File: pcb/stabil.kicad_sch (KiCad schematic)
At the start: 44 parts, among them Q10 IRFR5305, U11 TPS5430DDA, U12 LM75B, U13 INA219AxD, U14 LM78M05_TO252, U16 TSV911IDT, U17 PC817

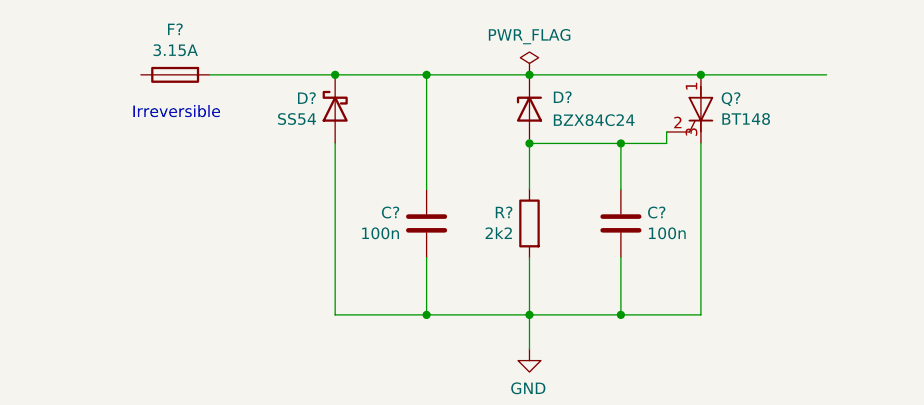
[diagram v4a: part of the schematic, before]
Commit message: Use normal SMD footprints, avoid handsolder.
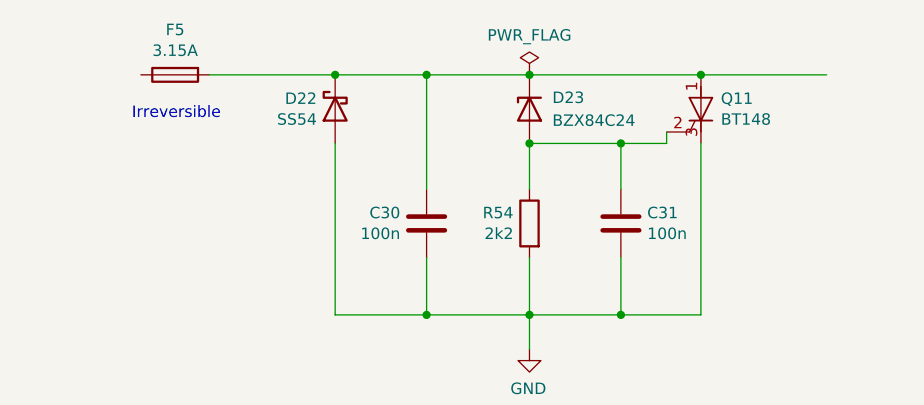
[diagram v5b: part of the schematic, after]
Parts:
- C14, C19, C21, C23, C24, C26, C27, C28: footprint Capacitor_SMD:C_0805_2012Metric_Pad1.18x1.45mm_HandSolder -> Capacitor_SMD:C_0805_2012Metric
- C30, C31: renamed from C?; footprint Capacitor_SMD:C_0805_2012Metric_Pad1.18x1.45mm_HandSolder -> Capacitor_SMD:C_0805_2012Metric
- D17: footprint Diode_SMD:D_SMA_Handsoldering -> Diode_SMD:D_SMA
- D22: renamed from D?; footprint Diode_SMD:D_SMA_Handsoldering -> Diode_SMD:D_SMA
- R30, R33, R44, R45, R46, R52, R53, R56, R57, R58: footprint Resistor_SMD:R_0805_2012Metric_Pad1.20x1.40mm_HandSolder -> Resistor_SMD:R_0805_2012Metric
- R43, R55: footprint Resistor_SMD:R_2512_6332Metric_Pad1.40x3.35mm_HandSolder -> Resistor_SMD:R_2512_6332Metric
- R54: renamed from R?; footprint Resistor_SMD:R_0805_2012Metric_Pad1.20x1.40mm_HandSolder -> Resistor_SMD:R_0805_2012Metric
- gave numbers to parts that had none: 3
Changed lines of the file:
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@@
 			)
 		)
-		(property "Footprint" "Resistor_SMD:R_0805_2012Metric_Pad1.20x1.40mm_HandSolder"
+		(property "Footprint" "Resistor_SMD:R_0805_2012Metric"
 			(at 202.692 36.83 90)
 			(effects
@@
 			)
 		)
-		(property "Footprint" "Resistor_SMD:R_0805_2012Metric_Pad1.20x1.40mm_HandSolder"
+		(property "Footprint" "Resistor_SMD:R_0805_2012Metric"
 			(at 223.012 36.83 90)
 			(effects
@@
 		(on_board yes)
 		(dnp no)
-		(property "Reference" "Q?"
+		(property "Reference" "Q11"
 			(at 215.5698 -37.9984 0)
 			(effects
@@
 			(project ""
 				(path "/99e6b8eb-b08e-4d42-84dd-8b7f6765b7b7/00000000-0000-0000-0000-000062367840"
-					(reference "Q?")
+					(reference "Q11")
 					(unit 1)
 				)
@@
 		(on_board yes)
 		(dnp no)
-		(property "Reference" "C?"
+		(property "Reference" "C31"
 			(at 207.391 -25.2984 0)
 			(effects
@@
 			)
 		)
-		(property "Footprint" "Capacitor_SMD:C_0805_2012Metric_Pad1.18x1.45mm_HandSolder"
+		(property "Footprint" "Capacitor_SMD:C_0805_2012Metric"
 			(at 203.5048 -27.94 0)
 			(effects
@@
 			(project ""
 				(path "/99e6b8eb-b08e-4d42-84dd-8b7f6765b7b7/00000000-0000-0000-0000-000062367840"
-					(reference "C?")
+					(reference "C31")
 					(unit 1)
 				)
@@
 		(on_board yes)
 		(dnp no)
-		(property "Reference" "R?"
+		(property "Reference" "R54"
 			(at 192.532 -25.2984 0)
 			(effects
@@
 			)
 		)
-		(property "Footprint" "Resistor_SMD:R_0805_2012Metric_Pad1.20x1.40mm_HandSolder"
+		(property "Footprint" "Resistor_SMD:R_0805_2012Metric"
 			(at 196.088 -24.13 90)
 			(effects
@@
 			(project ""
 				(path "/99e6b8eb-b08e-4d42-84dd-8b7f6765b7b7/00000000-0000-0000-0000-000062367840"
-					(reference "R?")
+					(reference "R54")
 					(unit 1)
 				)
@@
 		(on_board yes)
 		(dnp no)
-		(property "Reference" "C?"
+		(property "Reference" "C30"
 			(at 179.959 -25.2984 0)
 			(effects
@@
 			)
 		)
-		(property "Footprint" "Capacitor_SMD:C_0805_2012Metric_Pad1.18x1.45mm_HandSolder"
+		(property "Footprint" "Capacitor_SMD:C_0805_2012Metric"
 			(at 181.9148 -20.32 0)
 			(effects
@@
 			(project ""
 				(path "/99e6b8eb-b08e-4d42-84dd-8b7f6765b7b7/00000000-0000-0000-0000-000062367840"
-					(reference "C?")
+					(reference "C30")
 					(unit 1)
 				)
@@
 		(on_board yes)
 		(dnp no)
-		(property "Reference" "D?"
+		(property "Reference" "D23"
 			(at 196.85 -38.1 90)
 			(effects
@@
 			(project ""
 				(path "/99e6b8eb-b08e-4d42-84dd-8b7f6765b7b7/00000000-0000-0000-0000-000062367840"
-					(reference "D?")
+					(reference "D23")
 					(unit 1)
 				)
@@
 		(on_board yes)
 		(dnp no)
-		(property "Reference" "F?"
+		(property "Reference" "F5"
 			(at 154.94 -45.6438 90)
 			(effects
@@
 			(project ""
 				(path "/99e6b8eb-b08e-4d42-84dd-8b7f6765b7b7/00000000-0000-0000-0000-000062367840"
-					(reference "F?")
+					(reference "F5")
 					(unit 1)
 				)
@@
 		(on_board yes)
 		(dnp no)
-		(property "Reference" "#PWR?"
+		(property "Reference" "#PWR012"
 			(at 194.31 -3.81 0)
 			(effects
@@
 			(project ""
 				(path "/99e6b8eb-b08e-4d42-84dd-8b7f6765b7b7/00000000-0000-0000-0000-000062367840"
-					(reference "#PWR?")
+					(reference "#PWR012")
 					(unit 1)
 				)
@@
 		(on_board yes)
 		(dnp no)
-		(property "Reference" "#FLG?"
+		(property "Reference" "#FLG01"
 			(at 194.31 -42.545 0)
 			(effects
@@
 			(project ""
 				(path "/99e6b8eb-b08e-4d42-84dd-8b7f6765b7b7/00000000-0000-0000-0000-000062367840"
-					(reference "#FLG?")
+					(reference "#FLG01")
 					(unit 1)
 				)
@@
 		(on_board yes)
 		(dnp no)
-		(property "Reference" "D?"
+		(property "Reference" "D22"
 			(at 170.688 -37.9984 90)
 			(effects
@@
 			)
 		)
-		(property "Footprint" "Diode_SMD:D_SMA_Handsoldering"
+		(property "Footprint" "Diode_SMD:D_SMA"
 			(at 172.72 -36.83 0)
 			(effects
@@
 			(project ""
 				(path "/99e6b8eb-b08e-4d42-84dd-8b7f6765b7b7/00000000-0000-0000-0000-000062367840"
-					(reference "D?")
+					(reference "D22")
 					(unit 1)
 				)
@@
 			)
 		)
-		(property "Footprint" "Resistor_SMD:R_0805_2012Metric_Pad1.20x1.40mm_HandSolder"
+		(property "Footprint" "Resistor_SMD:R_0805_2012Metric"
 			(at 66.04 54.102 90)
 			(effects
@@
 			)
 		)
-		(property "Footprint" "Resistor_SMD:R_2512_6332Metric_Pad1.40x3.35mm_HandSolder"
+		(property "Footprint" "Resistor_SMD:R_2512_6332Metric"
 			(at 182.372 81.28 90)
 			(effects
@@
 			)
 		)
-		(property "Footprint" "Resistor_SMD:R_0805_2012Metric_Pad1.20x1.40mm_HandSolder"
+		(property "Footprint" "Resistor_SMD:R_0805_2012Metric"
 			(at 247.142 82.55 90)
 			(effects
@@
 			)
 		)
-		(property "Footprint" "Resistor_SMD:R_0805_2012Metric_Pad1.20x1.40mm_HandSolder"
+		(property "Footprint" "Resistor_SMD:R_0805_2012Metric"
 			(at 259.842 105.41 90)
 			(effects
@@
 			)
 		)
-		(property "Footprint" "Capacitor_SMD:C_0805_2012Metric_Pad1.18x1.45mm_HandSolder"
+		(property "Footprint" "Capacitor_SMD:C_0805_2012Metric"
 			(at 79.7052 177.8 0)
 			(effects
@@
 			)
 		)
-		(property "Footprint" "Capacitor_SMD:C_0805_2012Metric_Pad1.18x1.45mm_HandSolder"
+		(property "Footprint" "Capacitor_SMD:C_0805_2012Metric"
 			(at 115.2652 177.8 0)
 			(effects
@@
 			)
 		)
-		(property "Footprint" "Capacitor_SMD:C_0805_2012Metric_Pad1.18x1.45mm_HandSolder"
+		(property "Footprint" "Capacitor_SMD:C_0805_2012Metric"
 			(at 59.3852 40.64 0)
 			(effects
@@
 			)
 		)
-		(property "Footprint" "Resistor_SMD:R_0805_2012Metric_Pad1.20x1.40mm_HandSolder"
+		(property "Footprint" "Resistor_SMD:R_0805_2012Metric"
 			(at 76.962 46.99 90)
 			(effects
@@
 			)
 		)
-		(property "Footprint" "Capacitor_SMD:C_0805_2012Metric_Pad1.18x1.45mm_HandSolder"
+		(property "Footprint" "Capacitor_SMD:C_0805_2012Metric"
 			(at 114.3 31.4452 0)
 			(effects
@@
 			)
 		)
-		(property "Footprint" "Diode_SMD:D_SMA_Handsoldering"
+		(property "Footprint" "Diode_SMD:D_SMA"
 			(at 132.08 36.83 0)
 			(effects
@@
 			)
 		)
-		(property "Footprint" "Resistor_SMD:R_0805_2012Metric_Pad1.20x1.40mm_HandSolder"
+		(property "Footprint" "Resistor_SMD:R_0805_2012Metric"
 			(at 169.672 36.83 90)
 			(effects
@@
 			)
 		)
-		(property "Footprint" "Resistor_SMD:R_2512_6332Metric_Pad1.40x3.35mm_HandSolder"
+		(property "Footprint" "Resistor_SMD:R_2512_6332Metric"
 			(at 214.63 28.702 90)
 			(effects
@@
 			)
 		)
-		(property "Footprint" "Capacitor_SMD:C_0805_2012Metric_Pad1.18x1.45mm_HandSolder"
+		(property "Footprint" "Capacitor_SMD:C_0805_2012Metric"
 			(at 157.1752 102.87 0)
 			(effects
@@
 			)
 		)
-		(property "Footprint" "Resistor_SMD:R_0805_2012Metric_Pad1.20x1.40mm_HandSolder"
+		(property "Footprint" "Resistor_SMD:R_0805_2012Metric"
 			(at 173.228 66.04 90)
 			(effects
@@
 			)
 		)
-		(property "Footprint" "Capacitor_SMD:C_0805_2012Metric_Pad1.18x1.45mm_HandSolder"
+		(property "Footprint" "Capacitor_SMD:C_0805_2012Metric"
 			(at 84.7852 77.47 0)
 			(effects
@@
 			)
 		)
-		(property "Footprint" "Resistor_SMD:R_0805_2012Metric_Pad1.20x1.40mm_HandSolder"
+		(property "Footprint" "Resistor_SMD:R_0805_2012Metric"
 			(at 202.692 64.77 90)
 			(effects
@@
 			)
 		)
-		(property "Footprint" "Capacitor_SMD:C_0805_2012Metric_Pad1.18x1.45mm_HandSolder"
+		(property "Footprint" "Capacitor_SMD:C_0805_2012Metric"
 			(at 213.0552 66.04 0)
 			(effects
@@
 			)
 		)
-		(property "Footprint" "Capacitor_SMD:C_0805_2012Metric_Pad1.18x1.45mm_HandSolder"
+		(property "Footprint" "Capacitor_SMD:C_0805_2012Metric"
 			(at 257.5052 60.96 0)
 			(effects
@@
 			)
 		)
-		(property "Footprint" "Resistor_SMD:R_0805_2012Metric_Pad1.20x1.40mm_HandSolder"
+		(property "Footprint" "Resistor_SMD:R_0805_2012Metric"
 			(at 69.088 83.82 90)
 			(effects

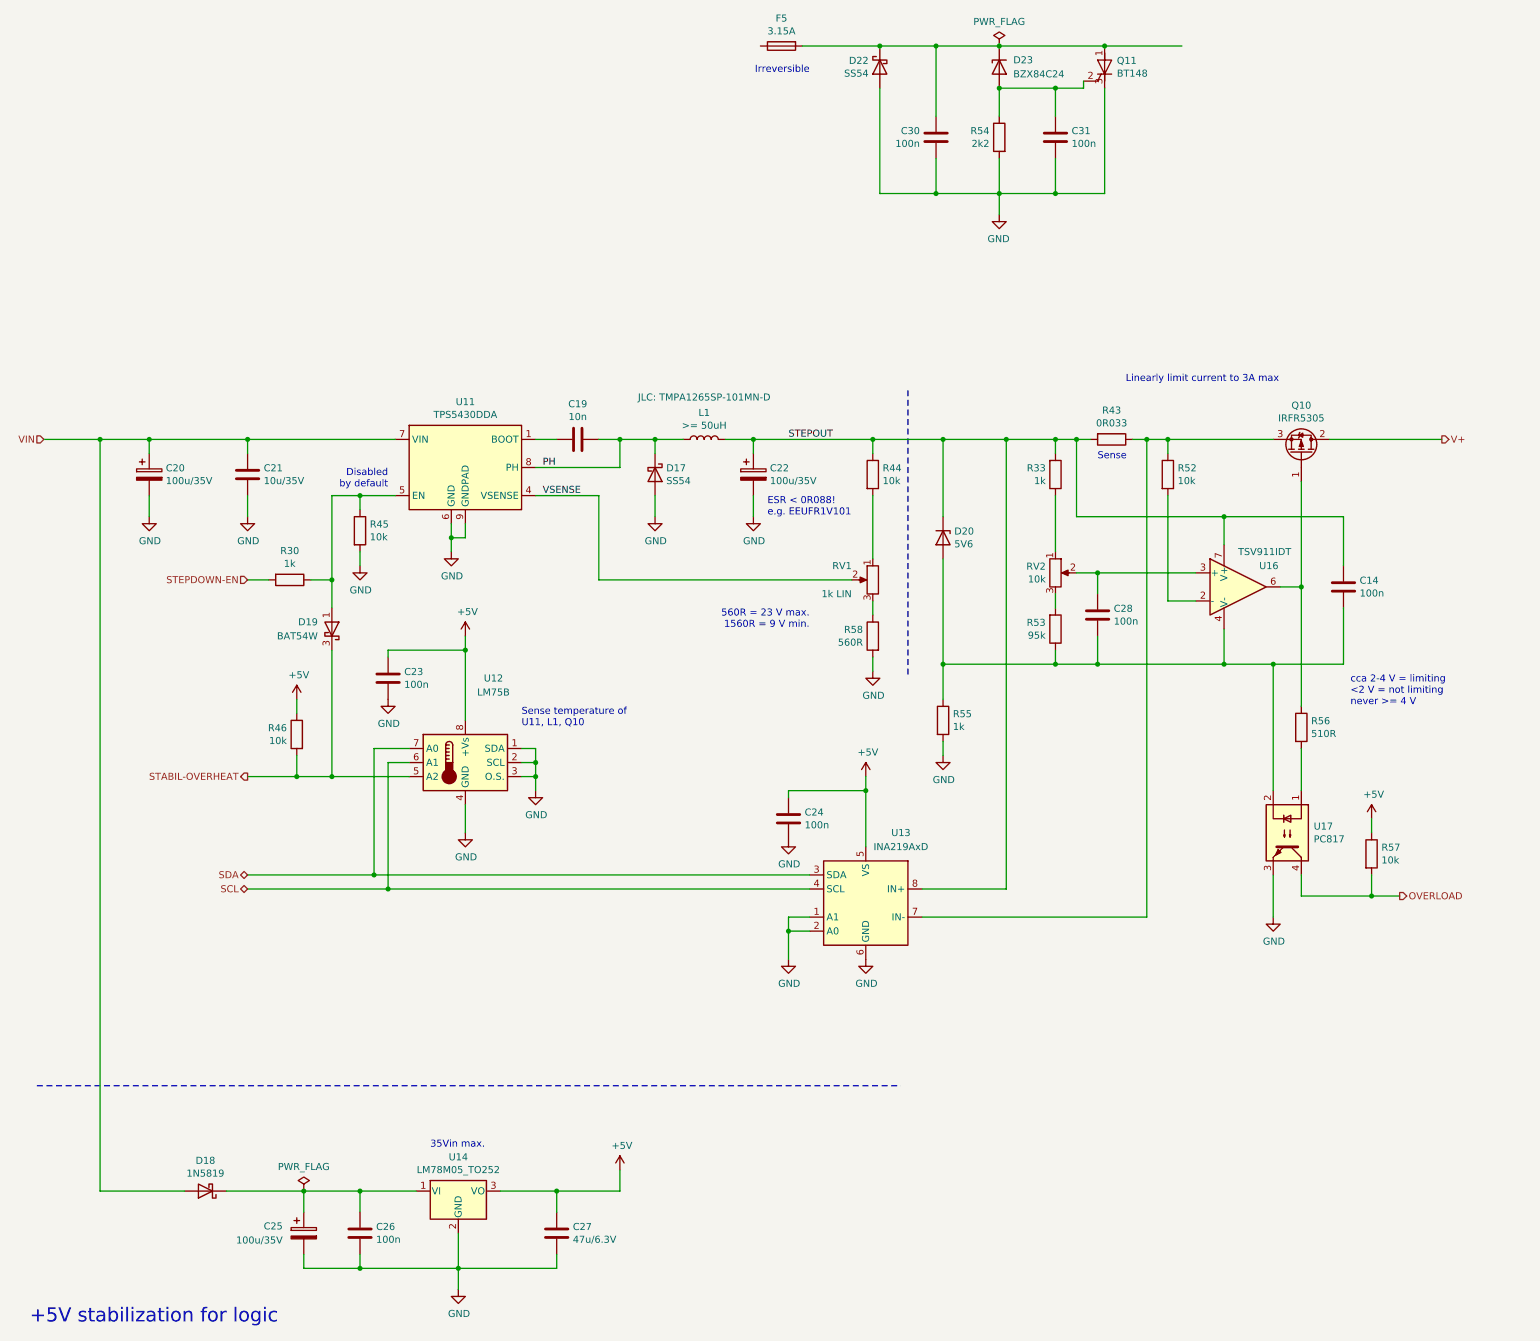
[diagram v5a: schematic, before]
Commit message: Add stabil heatsinks, minor improvements.
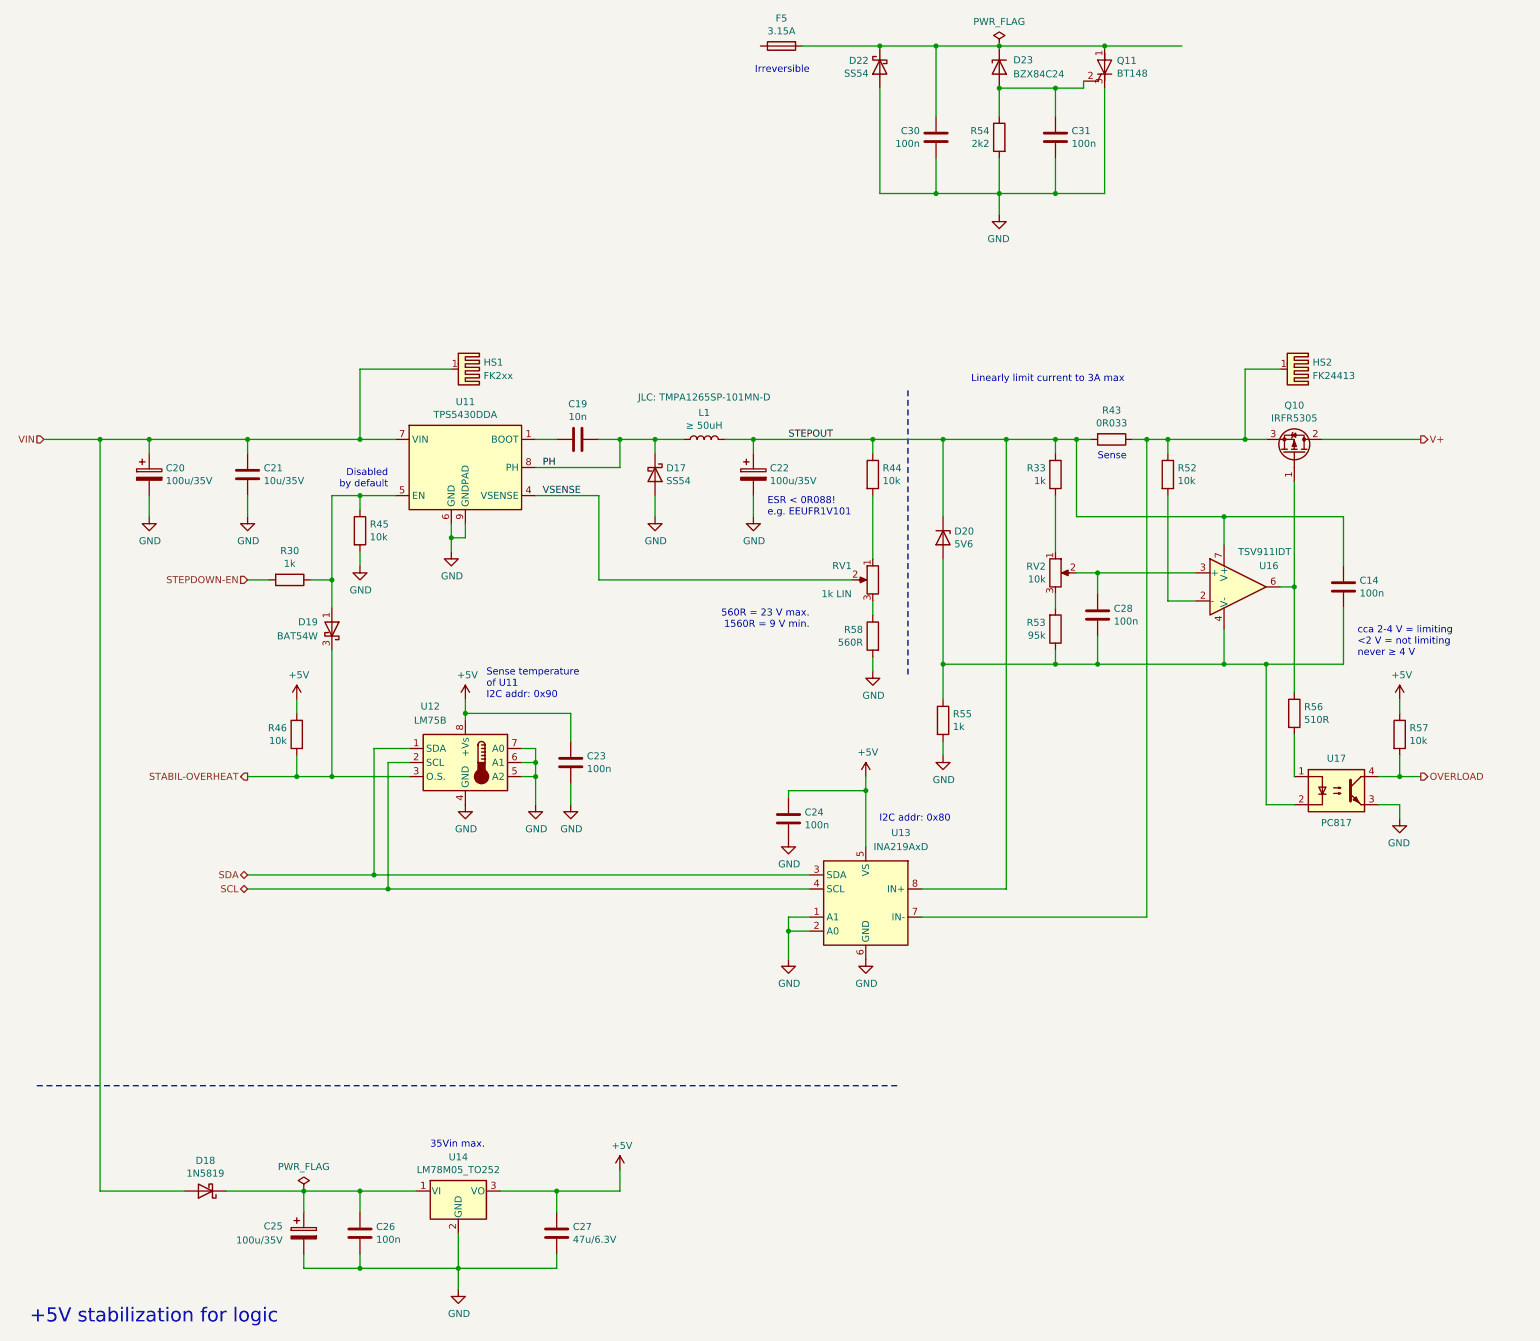
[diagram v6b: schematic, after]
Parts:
- added HS1: FK2xx, Heatsink:Heatsink_Fischer_FK24413DPAK_23x13mm, symbol Mechanical:Heatsink_Pad
- added HS2: FK24413, Heatsink:Heatsink_Fischer_FK24413DPAK_23x13mm, symbol Mechanical:Heatsink_Pad
- L1: value >= 50uH -> ≥ 50uH
- U17: footprint Package_DIP:DIP-4_W7.62mm -> Package_DIP:DIP-4_W8.89mm_SMDSocket_LongPads
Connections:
- net GND: now also U12.5 (A2), U12.6 (A1), U12.7 (A0); no longer U12.1 (SDA), U12.2 (SCL), U12.3 (O.S.)
- net SCL: now also U12.2 (SCL); no longer U12.6 (A1)
- net SDA: now also U12.1 (SDA); no longer U12.7 (A0)
- net STABIL-OVERHEAT: now also U12.3 (O.S.); no longer U12.5 (A2)
- net VIN: now also HS1.1
- net at Q10.3 (S), R43.1, R52.1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: now also HS2.1
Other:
- note added: "I2C addr: 0x80"
- note added: "Sense temperature of U11 I2C addr: 0x90"
- note added: "cca 2-4 V = limiting <2 V = not limiting never ≥ 4 V"
- note removed: "Sense temperature of U11, L1, Q10"
- note removed: "cca 2-4 V = limiting <2 V = not limiting never >= 4 V"
- moved on the sheet: C23, Q10, R56, R57, U17
